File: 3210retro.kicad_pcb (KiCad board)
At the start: 2 copper layers, 44 x 115 mm, 404 parts, among them J901 MICRO_SD, P101 USB_OTG, P102 BAT, P103 DC, P105 EAR, P107 HEADPHONE, P109 RUMBLE, P301 SEPS525, P801 JTAG, Q201 BC817-40, Q801 BSS138, SW701 SW_PUSH, SW702 C, SW703 1, SW704 4ghi, SW705 7pqrs, SW706 -, SW707 2abc, SW708 5jkl, SW709 8tuv, SW710 UP, SW711 3def, SW712 6mno, SW713 9wxyz, SW714 *+, SW715 DOWN, SW716 0space, SW717 #up, U201 STM32F439NIH6, U202 TPS61046, U302 TPS61041DBV, U401 TPS62172, U402 MAX1555, U403 DRV8601, U404 LM4930, U405 TS5A22366, U406 MP34DT01TR, U407 MP34DT01TR, U801 A7, U802 SIM_SLOT, U901 ESP-12E, X101 ANT_GPS, X102 ANT_GSM, Y201 32kHz, Y202 24MHz, Y401 1M

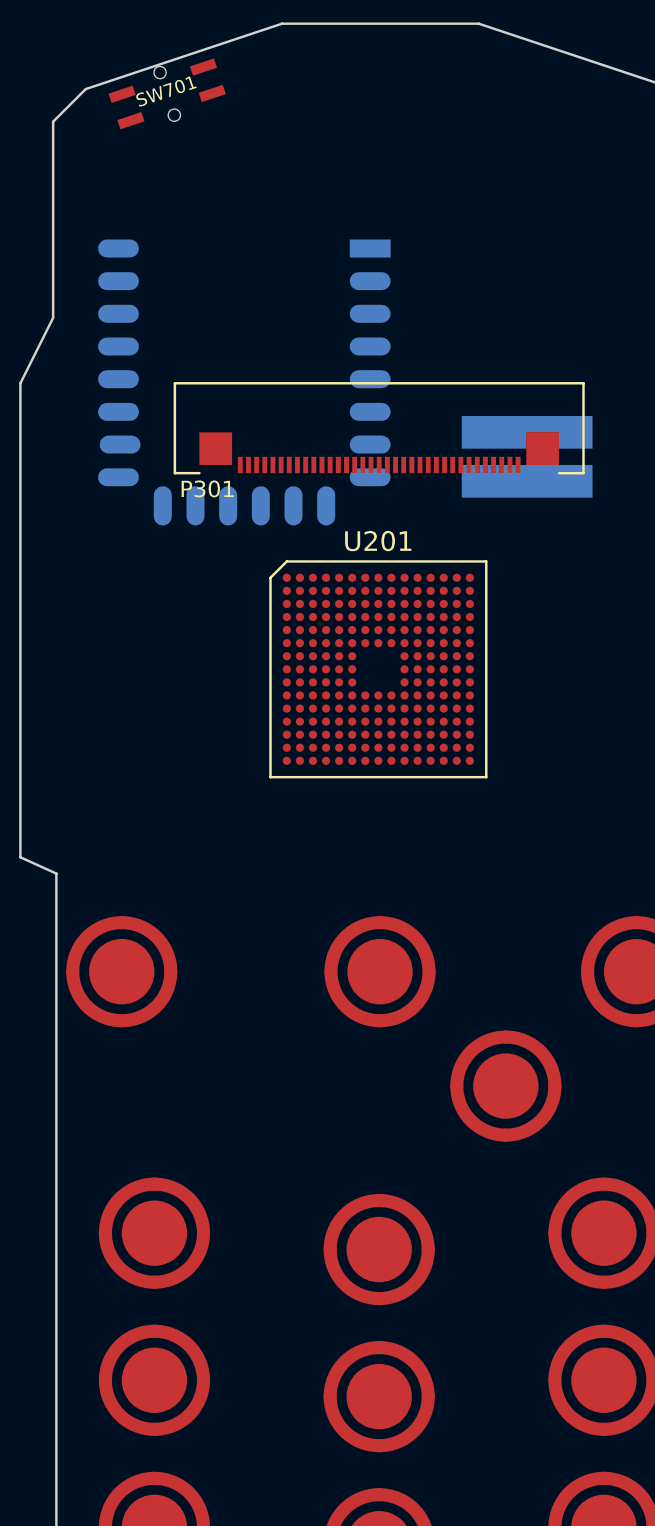
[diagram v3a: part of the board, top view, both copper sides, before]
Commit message: Started STM32 Fanout
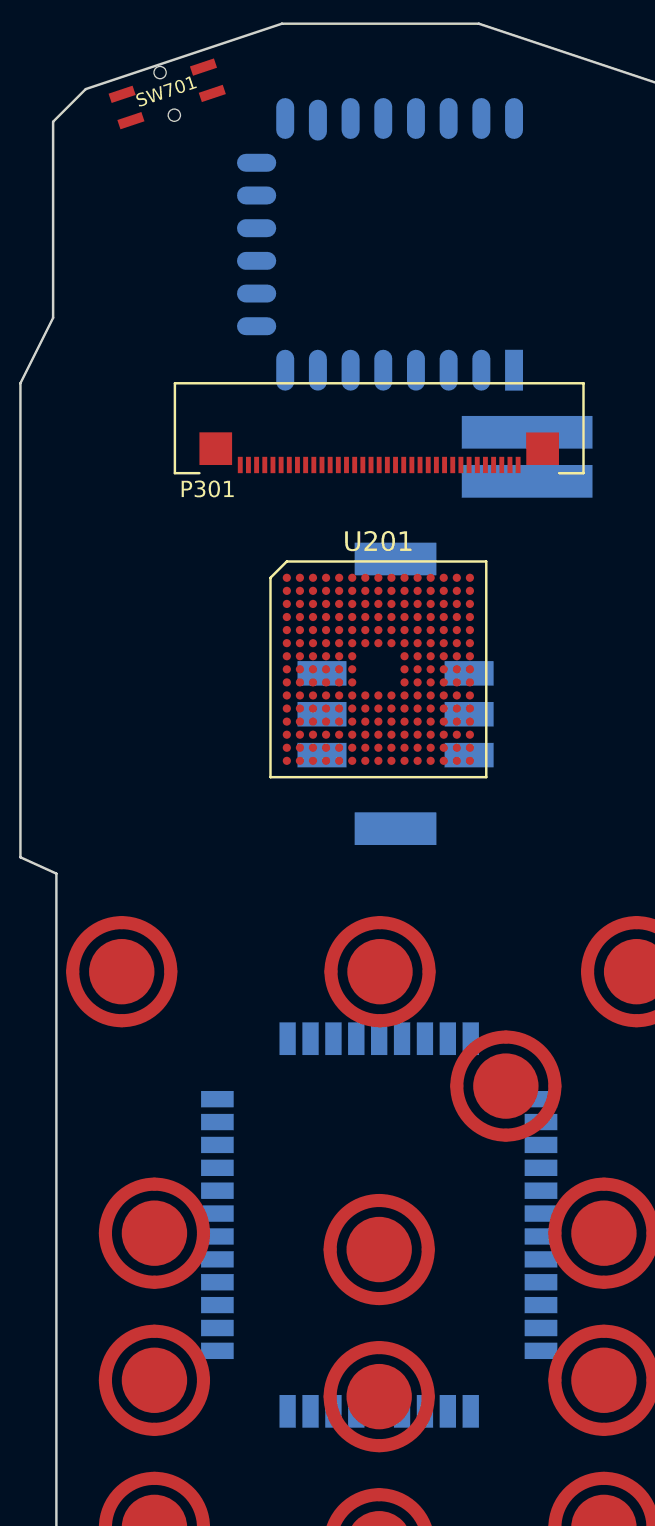
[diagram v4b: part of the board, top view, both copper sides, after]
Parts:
- moved U801 19.3 mm to (99.3, 117.6)
- moved U901 11.7 mm to (107.6, 64.6), turned to 90 degrees
- moved U802 5.76 mm to (100.3, 85.1), turned to 180 degrees
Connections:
- R803 pad 1: (no net) -> Net-(R803-Pad1)
- R804 pad 1: (no net) -> Net-(R804-Pad1)
- R805 pad 1: (no net) -> Net-(R805-Pad1)
- R806 pad 1: (no net) -> Net-(R806-Pad1)
- R807 pad 1: (no net) -> Net-(R807-Pad1)
- R808 pad 1: (no net) -> Net-(R808-Pad1)
- R809 pad 1: (no net) -> Net-(R809-Pad1)
- R810 pad 1: (no net) -> Net-(R810-Pad1)
- R813 pad 2: (no net) -> Net-(R813-Pad2)
- U404 pad 24: (no net) -> /Audio Amplifier/SPK_-
- U404 pad 25: (no net) -> /Audio Amplifier/SPK_+
- U405 pad D1: (no net) -> /Audio Amplifier/MIC_-
- U405 pad D3: (no net) -> /Audio Amplifier/MIC_+

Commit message: placed leds and corrected measurements
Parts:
- R234, R235: moved to B.Cu
- U201: footprint buttons:STM32F439NI -> buttons:STM32F439NI2
- moved C209 286.5 mm to (-100.7, 194.0)
- moved C218 285.6 mm to (-101.6, 180.4)
- moved C208 285.0 mm to (-106.6, 198.8)
- moved C207 283.3 mm to (-107.4, 190.7)
- moved C212 277.5 mm to (-94.0, 189.6)
- moved C220 274.0 mm to (-96.7, 179.1)
- moved C210 272.1 mm to (-98.9, 187.9)
- moved C225 271.7 mm to (-100.6, 174.2)
- moved C223 271.3 mm to (-95.9, 171.1)
- moved C221 269.5 mm to (-88.5, 176.4)
- moved C214 268.4 mm to (-90.0, 181.1)
- moved C222 265.4 mm to (-94.6, 176.0)
- moved C224 262.3 mm to (-91.0, 172.7)
- moved C216 262.2 mm to (-94.6, 194.3)
- moved C217 260.6 mm to (-89.4, 191.3)
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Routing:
- net (no net): track 0.00 -> 154.4 mm, vias 0 -> 37
- net GND: track 0.00 -> 45.7 mm, vias 0 -> 8
- net VCC: track 0.00 -> 41.9 mm, vias 0 -> 10
- net /Buttons and LEDs/KEY0: track 0.00 -> 34.8 mm, vias 0 -> 4
- net Net-(R234-Pad1): track 0.00 -> 11.5 mm
- net Net-(R237-Pad1): track 0.00 -> 5.67 mm, vias 0 -> 1
- net Net-(R247-Pad1): track 0.00 -> 5.13 mm, vias 0 -> 1
- net Net-(R236-Pad1): track 0.00 -> 5.03 mm, vias 0 -> 1
- net Net-(P801-Pad10): track 0.00 -> 4.95 mm, vias 0 -> 2
- net Net-(RP905-Pad2): track 0.00 -> 4.27 mm
- net Net-(RP905-Pad1): track 0.00 -> 4.07 mm, vias 0 -> 1
- net Net-(R248-Pad1): track 0.00 -> 3.77 mm, vias 0 -> 1
- net Net-(R246-Pad1): track 0.00 -> 3.57 mm, vias 0 -> 1
- net Net-(C206-Pad1): track 0.00 -> 3.49 mm, vias 0 -> 2
- net Net-(RP903-Pad5): track 0.00 -> 3.07 mm
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- added copper zone on F.Cu, net GND
- added copper zone on In1.Cu, net GND
- added copper zone on F.Cu, net VCC
- added copper zone on In2.Cu, net VCC
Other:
- board size 44 x 115 mm -> 44 x 118 mm
- copper layers 2 -> 4
- net class Default: clearance 0.2 -> 0.15; trace_width 0.25 -> 0.15; via_dia 0.6 -> 0.5; via_drill 0.4 -> 0.2
- net class SmallPower added: clearance 0.15, trace_width 0.2, via_dia 0.5, via_drill 0.2
- rule trace_clearance: 0.2 -> 0.15
- rule trace_min: 0.2 -> 0.15
- rule via_min_drill: 0.3 -> 0.2

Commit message: Created netlist with current components Foreward Annotation to Board
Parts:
- removed C221, C222, C223, C224, C225, C227, C306, C307, C308, C309, C423, C424, C425, C426: 100n, Capacitors_SMD:C_0603
- removed C226: 10u, Capacitors_SMD:C_0603
- removed C228: 1n, Capacitors_SMD:C_0603
- removed C229, C230, C231, C312: 1u, Capacitors_SMD:C_0603
- removed C310: 4u7C, Capacitors_SMD:C_0603
- removed C311: 10p, Capacitors_SMD:C_0603
- removed FI401: EMI_FILTER2, Choke_SMD:Choke_SMD_1206_Standard
- removed Q801: BSS138, TO_SOT_Packages_SMD:SOT-23
- removed R219, R220, R221, R222, R225, R226, R228, R229, R234, R235, R236, R237, R238, R239, R240, R241, R242, R243, R244, R245, R246, R247, R248, R816, R817, R818: 100, Resistors_SMD:R_0603
- removed R223, R224, R408, R409, R410, R412, R413, R414, R415: R, Resistors_SMD:R_0603
- removed R227: 10k, Resistors_SMD:R_0603
- removed R249, R416: 0, Resistors_SMD:R_0603
- removed R411, R417: 50k, Resistors_SMD:R_0603
- removed R418: 100k, Resistors_SMD:R_0603
- removed R419, R420: 1k, Resistors_SMD:R_0603
- removed R710, R712: 280, Resistors_SMD:R_0603
- removed R911, R912, R913, R915, R916: 10, Resistors_SMD:R_0603
- removed R914: 22, Resistors_SMD:R_0603
- removed RP901, RP902, RP903, RP904, RP905: 100, Resistors_SMD:R_Array_Convex_8x0602
- removed TP207, TP208, TP209, TP210, TP211, TP212, TP213, TP214, TP215, TP216, TP502, TP503, TP504, TP505, TP506, TP507, TP508, TP509, TP510, TP511, TP512, TP513, TP514, TP515, TP601, TP602, TP734, TP735, TP736, TP737, TP738, TP739, TP740, TP741, TP742, TP743, TP744, TP745, TP746, TP747, TP748, TP802, TP803, TP804, TP805, TP806, TP807, TP808, TP809, TP810, TP811, TP812, TP813, TP814, TP815, TP816, TP817, TP818, TP819, TP820, TP821, TP822, TP823, TP824, TP825, TP826, TP827, TP828, TP829, TP830, TP831, TP832, TP833, TP834, TP835, TP836, TP837, TP838, TP839, TP840, TP841, TP842, TP843, TP844, TP845, TP846, TP847, TP848, TP849, TP850, TP851, TP852, TP853, TP854, TP855, TP856, TP901, TP902, TP903, TP904, TP905, TP906, TP907, TP908, TP909, TP910, TP911, TP912: TP, buttons:TP
- removed U302: TPS61041DBV, TO_SOT_Packages_SMD:SOT-23
- removed U406, U407: MP34DT01TR, buttons:MP34DT01
- removed U802: SIM_SLOT, buttons:SIM
- removed Y201: 32kHz, Crystals:Crystal_SMD_SeikoEpson_MC146-4pin_6.7x1.5mm_HandSoldering
- removed Y202: 24MHz, Crystals:Crystal_SMD_SeikoEpson_MC146-4pin_6.7x1.5mm_HandSoldering
- removed Y401: 1M, Crystals:Crystal_SMD_SeikoEpson_MC146-4pin_6.7x1.5mm_HandSoldering
- added BT1001: LI_BAT, Pin_Headers:Pin_Header_Straight_1x02, F.Cu at (383.7, 45.1)
- added C1001: 1u, Capacitors_SMD:C_0603, F.Cu at (386.1, 76.7)
- added C1002: 1u, Capacitors_SMD:C_0603, F.Cu at (415.5, 47.7)
- added C1003: 2u2, Capacitors_SMD:C_0603, F.Cu at (378.8, 70.1)
- added C1004: 1u, Capacitors_SMD:C_0603, F.Cu at (420.6, 41.9)
- added C1005: 4u7, Capacitors_SMD:C_0603, F.Cu at (409.6, 53.4)
- added C1006: 2u2, Capacitors_SMD:C_0603, F.Cu at (399.6, 64.9)
- added C1007: 10uF, Capacitors_SMD:C_0603, F.Cu at (404.7, 59.2)
- added C1008: 4u7, Capacitors_SMD:C_0603, F.Cu at (391.2, 72.0)
- added C1009: 100nF, Capacitors_SMD:C_0402, F.Cu at (435.9, 47.1)
- added C1010: 1uF, Capacitors_SMD:C_0603, F.Cu at (396.3, 72.0)
- added C1011: 2u2, Capacitors_SMD:C_0603, F.Cu at (420.6, 47.7)
- added C1012: 1uF, Capacitors_SMD:C_0603, F.Cu at (425.7, 41.9)
- added C1013: 4u7, Capacitors_SMD:C_0603, F.Cu at (414.7, 53.4)
- added C1014: 220nF, Capacitors_SMD:C_0402, F.Cu at (420.0, 58.8)
- added C1015: 1uF, Capacitors_SMD:C_0603, F.Cu at (394.5, 66.2)
- added C1016: 100nF, Capacitors_SMD:C_0402, F.Cu at (424.9, 53.2)
- added C1017: 100n, Capacitors_SMD:C_0402, F.Cu at (430.0, 53.0)
- added C1018: 4u7, Capacitors_SMD:C_0603, F.Cu at (389.4, 66.2)
- added C1019: 100nF, Capacitors_SMD:C_0402, F.Cu at (420.0, 64.1)
- added C1020: 100n, Capacitors_SMD:C_0402, F.Cu at (414.9, 64.5)
- added C1021: 100n, Capacitors_SMD:C_0402, F.Cu at (409.8, 64.5)
- added C1022: 1u, Capacitors_SMD:C_0603, F.Cu at (415.5, 41.9)
- added C1023: 100n, Capacitors_SMD:C_0402, F.Cu at (430.8, 47.3)
- added C1024: 100n, Capacitors_SMD:C_0402, F.Cu at (435.9, 41.7)
- added C1025: 100n, Capacitors_SMD:C_0402, F.Cu at (401.4, 76.0)
- added C1026: 100n, Capacitors_SMD:C_0402, F.Cu at (406.5, 70.3)
- added C1027: 4u7, Capacitors_SMD:C_0603, F.Cu at (410.4, 47.7)
- added C1028: 4u7, Capacitors_SMD:C_0603, F.Cu at (381.0, 76.7)
- added C1029: 4u7, Capacitors_SMD:C_0603, F.Cu at (399.6, 59.2)
- added C1030: 4u7, Capacitors_SMD:C_0603, F.Cu at (384.3, 65.2)
- added C1031: 22uF, Capacitors_SMD:C_0603, F.Cu at (384.3, 59.5)
- added C1032: 22u, Capacitors_SMD:C_0603, F.Cu at (394.3, 54.7)
- added C1033: 22u, Capacitors_SMD:C_0603, F.Cu at (394.3, 49.0)
- added C1034: 22uF, Capacitors_SMD:C_0603, F.Cu at (400.2, 47.7)
- added C1035: 22u, Capacitors_SMD:C_0603, F.Cu at (400.2, 41.9)
- added C1036: 22u, Capacitors_SMD:C_0603, F.Cu at (405.3, 47.7)
- added C1037: 22u, Capacitors_SMD:C_0603, F.Cu at (405.3, 41.9)
- added C1038: 22u, Capacitors_SMD:C_0603, F.Cu at (410.4, 41.9)
- added C1039: 22u, Capacitors_SMD:C_0603, F.Cu at (399.4, 53.4)
- added C1040: 22u, Capacitors_SMD:C_0603, F.Cu at (389.4, 60.5)
- added C1041: 22u, Capacitors_SMD:C_0603, F.Cu at (375.9, 75.9)
- added C1042: 22u, Capacitors_SMD:C_0603, F.Cu at (383.9, 71.0)
- added C1043: 22u, Capacitors_SMD:C_0603, F.Cu at (394.5, 60.5)
- added C1044: 22u, Capacitors_SMD:C_0603, F.Cu at (404.5, 53.4)
- added C1101: 220n, Capacitors_SMD:C_0402, F.Cu at (502.1, 102.8)
- added C1102: 220n, Capacitors_SMD:C_0402, F.Cu at (497.0, 102.8)
- added C1103: 220n, Capacitors_SMD:C_0402, F.Cu at (502.1, 97.4)
- added C1104: 220n, Capacitors_SMD:C_0402, F.Cu at (497.0, 97.4)
- added C1105: 2u2, Capacitors_SMD:C_0603, F.Cu at (491.9, 97.6)
- added C1106: C, Capacitors_SMD:C_0402, F.Cu at (491.9, 103.2)
- added C1201: 220n, Capacitors_SMD:C_0402, F.Cu at (561.9, 7.59)
- added C1202: 220n, Capacitors_SMD:C_0402, F.Cu at (556.4, 13.1)
- added C1203: 220n, Capacitors_SMD:C_0402, F.Cu at (567.0, 2.24)
- added C1204: 220n, Capacitors_SMD:C_0402, F.Cu at (572.1, -3.11)
- added C1205: 220n, Capacitors_SMD:C_0402, F.Cu at (577.2, -8.46)
- added C1206: 220n, Capacitors_SMD:C_0402, F.Cu at (567.0, -3.11)
- added C1207: 220n, Capacitors_SMD:C_0402, F.Cu at (561.9, 12.9)
- added C1208: 4u7, Capacitors_SMD:C_0603, F.Cu at (536.0, 8.99)
- added C1209: 220n, Capacitors_SMD:C_0402, F.Cu at (577.2, -3.11)
- added C1210: 220n, Capacitors_SMD:C_0402, F.Cu at (551.3, 13.5)
- added C1211: 220n, Capacitors_SMD:C_0402, F.Cu at (572.1, 2.24)
- added C1212: 220n, Capacitors_SMD:C_0402, F.Cu at (530.9, 15.8)
- added C1213: 220n, Capacitors_SMD:C_0402, F.Cu at (561.9, -8.46)
- added C1214: 220n, Capacitors_SMD:C_0402, F.Cu at (536.0, 14.5)
- added C1215: 2u2, Capacitors_SMD:C_0603, F.Cu at (530.9, -1.23)
- added C1216: 220n, Capacitors_SMD:C_0402, F.Cu at (551.7, 2.84)
- added C1217: 22u, Capacitors_SMD:C_0603, F.Cu at (536.4, -8.26)
- added C1218: 220n, Capacitors_SMD:C_0402, F.Cu at (546.2, 13.9)
- added C1219: 220n, Capacitors_SMD:C_0402, F.Cu at (556.8, 7.79)
- added C1220: 22u, Capacitors_SMD:C_0603, F.Cu at (541.5, -8.26)
- added C1221: 22u, Capacitors_SMD:C_0603, F.Cu at (536.4, -2.51)
- added C1222: 220n, Capacitors_SMD:C_0402, F.Cu at (561.9, 2.24)
- added C1223: 2u2, Capacitors_SMD:C_0603, F.Cu at (541.5, -2.51)
- added C1224: 2u2, Capacitors_SMD:C_0603, F.Cu at (536.0, 3.24)
- added C1225: 2u2, Capacitors_SMD:C_0603, F.Cu at (546.6, -2.51)
- added C1226: 220n, Capacitors_SMD:C_0402, F.Cu at (556.8, -2.91)
- added C1227: 220n, Capacitors_SMD:C_0402, F.Cu at (572.1, -8.46)
- added C1228: 220n, Capacitors_SMD:C_0402, F.Cu at (567.0, -8.46)
- added C1229: 220n, Capacitors_SMD:C_0402, F.Cu at (556.8, 2.44)
- added C1230: 2u2, Capacitors_SMD:C_0603, F.Cu at (541.1, 3.24)
- added C1231: 220n, Capacitors_SMD:C_0402, F.Cu at (561.9, -3.11)
- added C1232: 220n, Capacitors_SMD:C_0402, F.Cu at (551.3, 8.19)
- added C1233: 220n, Capacitors_SMD:C_0402, F.Cu at (541.1, 14.3)
- added C1234: 2u2, Capacitors_SMD:C_0603, F.Cu at (551.7, -8.26)
- added C1235: 220n, Capacitors_SMD:C_0402, F.Cu at (546.2, 8.59)
- added C1236: 2u2, Capacitors_SMD:C_0603, F.Cu at (530.9, 4.52)
- added C1237: 2u2, Capacitors_SMD:C_0603, F.Cu at (530.9, 10.3)
- added C1238: 2u2, Capacitors_SMD:C_0603, F.Cu at (546.6, -8.26)
- added C1301: 220n, Capacitors_SMD:C_0402, F.Cu at (603.7, -8.46)
- added C1302: 220n, Capacitors_SMD:C_0402, F.Cu at (596.7, -2.71)
- added C1303: 2u2, Capacitors_SMD:C_0603, F.Cu at (586.5, -4.31)
- added C1304: 2u2, Capacitors_SMD:C_0603, F.Cu at (593.5, -8.26)
- added C1305: 220n, Capacitors_SMD:C_0402, F.Cu at (601.8, -2.91)
- added C1306: 220n, Capacitors_SMD:C_0402, F.Cu at (608.8, -8.46)
- added C1307: 10u, Capacitors_SMD:C_0603, F.Cu at (586.5, 1.44)
- added C1308: 10n, Capacitors_SMD:C_0603, F.Cu at (591.6, -2.51)
- added C1309: 100n, Capacitors_SMD:C_0402, F.Cu at (606.9, -3.11)
- added C501: 100n, Capacitors_SMD:C_0402, F.Cu at (552.5, 71.5)
- added C502: 470u, Capacitors_SMD:C_0603, F.Cu at (544.2, 66.2)
- added C503: 100n, Capacitors_SMD:C_0402, F.Cu at (539.2, 84.8)
- added C504: C, Capacitors_SMD:C_0402, F.Cu at (548.3, 82.4)
- added C505: C, Capacitors_SMD:C_0402, F.Cu at (548.3, 77.1)
- added C506: C, Capacitors_SMD:C_0402, F.Cu at (552.5, 76.9)
- added C507: C, Capacitors_SMD:C_0402, F.Cu at (544.2, 82.8)
- added C601: 100n, Capacitors_SMD:C_0402, F.Cu at (413.4, 103.3)
- added C602: 1p, Capacitors_SMD:C_0402, F.Cu at (401.5, 115.1)
- added C603: 2p4, Capacitors_SMD:C_0402, F.Cu at (417.6, 103.1)
- added C604: 1u, Capacitors_SMD:C_0603, F.Cu at (409.3, 95.8)
- added C605: 10u, Capacitors_SMD:C_0603, F.Cu at (413.4, 86.7)
- added C606: 100n, Capacitors_SMD:C_0402, F.Cu at (405.7, 112.5)
- added C808: 2u2, Capacitors_SMD:C_0603, F.Cu at (535.3, 34.4)
- added C809: 100n, Capacitors_SMD:C_0402, F.Cu at (547.8, 39.8)
- added C810: 220n, Capacitors_SMD:C_0402, F.Cu at (535.0, 56.8)
- added C811: 470n, Capacitors_SMD:C_0402, F.Cu at (556.1, 34.2)
- added C812: 470n, Capacitors_SMD:C_0402, F.Cu at (543.6, 45.3)
- added C813: 470n, Capacitors_SMD:C_0402, F.Cu at (539.2, 56.2)
- added C814: 2u2, Capacitors_SMD:C_0603, F.Cu at (531.2, 34.4)
- added C815: 2u2, Capacitors_SMD:C_0603, F.Cu at (515.2, 55.6)
- added C816: 470n, Capacitors_SMD:C_0402, F.Cu at (556.1, 39.6)
- added C817: 470n, Capacitors_SMD:C_0402, F.Cu at (547.8, 50.5)
- added C818: 2u2, Capacitors_SMD:C_0603, F.Cu at (531.2, 40.2)
- added C905: 220n, Capacitors_SMD:C_0402, F.Cu at (476.6, 41.7)
- added C906: 22u, Capacitors_SMD:C_0603, F.Cu at (464.2, 47.7)
- added C907: 100n, Capacitors_SMD:C_0402, F.Cu at (463.7, 58.8)
- added C908: 220n, Capacitors_SMD:C_0402, F.Cu at (480.8, 41.7)
- added C909: 220n, Capacitors_SMD:C_0402, F.Cu at (459.6, 61.7)
- added C910: 220n, Capacitors_SMD:C_0402, F.Cu at (451.3, 67.5)
- added C911: 220n, Capacitors_SMD:C_0402, F.Cu at (472.5, 52.8)
- added C912: 220n, Capacitors_SMD:C_0402, F.Cu at (480.8, 63.1)
- added C913: 220n, Capacitors_SMD:C_0402, F.Cu at (476.6, 47.1)
- added C914: 220n, Capacitors_SMD:C_0402, F.Cu at (463.7, 64.1)
- added C915: 220n, Capacitors_SMD:C_0402, F.Cu at (480.8, 47.1)
- added C916: 220n, Capacitors_SMD:C_0402, F.Cu at (468.3, 58.2)
- added C917: 220n, Capacitors_SMD:C_0402, F.Cu at (459.6, 67.1)
- added C918: 220n, Capacitors_SMD:C_0402, F.Cu at (484.9, 41.7)
- added C919: 220n, Capacitors_SMD:C_0402, F.Cu at (472.5, 58.2)
- added C920: 220n, Capacitors_SMD:C_0402, F.Cu at (467.9, 63.5)
- added C921: 220n, Capacitors_SMD:C_0402, F.Cu at (484.9, 47.1)
- added C922: 220n, Capacitors_SMD:C_0402, F.Cu at (489.1, 41.7)
- added C923: 22u, Capacitors_SMD:C_0603, F.Cu at (451.3, 56.4)
- added C924: 22u, Capacitors_SMD:C_0603, F.Cu at (447.1, 62.1)
- added C925: 220n, Capacitors_SMD:C_0402, F.Cu at (480.8, 52.4)
- added C926: 220n, Capacitors_SMD:C_0402, F.Cu at (463.7, 69.5)
- added C927: 220n, Capacitors_SMD:C_0402, F.Cu at (468.3, 52.8)
- added C928: 220n, Capacitors_SMD:C_0402, F.Cu at (493.2, 41.7)
- added C929: 220n, Capacitors_SMD:C_0402, F.Cu at (476.6, 57.8)
- added C930: 220n, Capacitors_SMD:C_0402, F.Cu at (480.8, 57.8)
- added C931: 220n, Capacitors_SMD:C_0402, F.Cu at (467.9, 68.9)
- added C932: 220n, Capacitors_SMD:C_0402, F.Cu at (489.1, 52.4)
- added C933: 220n, Capacitors_SMD:C_0402, F.Cu at (489.1, 47.1)
- added C934: 220n, Capacitors_SMD:C_0402, F.Cu at (484.9, 52.4)
- added C935: 220n, Capacitors_SMD:C_0402, F.Cu at (472.0, 68.9)
- added C936: 220n, Capacitors_SMD:C_0402, F.Cu at (493.2, 47.1)
- added C937: 220n, Capacitors_SMD:C_0402, F.Cu at (476.6, 63.1)
- added C938: 22u, Capacitors_SMD:C_0603, F.Cu at (447.1, 56.4)
- added C939: 22u, Capacitors_SMD:C_0603, F.Cu at (464.2, 41.9)
- added C940: 220n, Capacitors_SMD:C_0402, F.Cu at (472.0, 63.5)
- added D1001: D_Schottky, Diodes_SMD:DD-PAK_TO263_SingleDiode, F.Cu at (374.3, 49.5)
- added D201: BZT52-C5V1, Diodes_SMD:DD-PAK_TO263_SingleDiode, F.Cu at (374.3, -0.71)
- added D202: MMSD914LT, Diodes_SMD:DD-PAK_TO263_SingleDiode, F.Cu at (374.3, 20.4)
- added D203: S1A, Diodes_SMD:DD-PAK_TO263_SingleDiode, F.Cu at (400.0, -0.71)
- added D204: MMSD914LT, Diodes_SMD:DD-PAK_TO263_SingleDiode, F.Cu at (412.9, -0.71)
- added D205: ZHCS1000, Diodes_SMD:DD-PAK_TO263_SingleDiode, F.Cu at (387.2, 20.4)
- added D206: MMSD914LT, Diodes_SMD:DD-PAK_TO263_SingleDiode, F.Cu at (400.0, 20.4)
- added D207: MMSD914LT, Diodes_SMD:DD-PAK_TO263_SingleDiode, F.Cu at (387.2, -0.71)
- added D401: D_TVS_ALT, Diodes_SMD:DD-PAK_TO263_SingleDiode, F.Cu at (461.2, -0.71)
- added D402: D_TVS_ALT, Diodes_SMD:DD-PAK_TO263_SingleDiode, F.Cu at (474.1, -0.71)
- added D403: D_TVS_ALT, Diodes_SMD:DD-PAK_TO263_SingleDiode, F.Cu at (486.9, -0.71)
- added D801: D_Schottky, Diodes_SMD:DD-PAK_TO263_SingleDiode, F.Cu at (514.1, 42.0)
- added J1001: TEST_1P, NokiaRetroFit:TP, F.Cu at (387.1, 46.7)
- added J902: GND, NokiaRetroFit:TP, F.Cu at (446.7, 71.2)
- added J903: GND, NokiaRetroFit:TP, F.Cu at (445.6, 71.2)
- added J904: GND, NokiaRetroFit:TP, F.Cu at (484.5, 55.7)
- added J905: GND, NokiaRetroFit:TP, F.Cu at (485.6, 55.7)
- added J906: GND, NokiaRetroFit:TP, F.Cu at (447.8, 71.2)
- added J907: GND, NokiaRetroFit:TP, F.Cu at (449.8, 70.8)
- added J908: GND, NokiaRetroFit:TP, F.Cu at (450.9, 70.8)
- added J909: GND, NokiaRetroFit:TP, F.Cu at (452.0, 70.8)
- added J910: GND, NokiaRetroFit:TP, F.Cu at (453.1, 70.8)
- added J911: GND, NokiaRetroFit:TP, F.Cu at (454.2, 70.6)
- added J912: GND, NokiaRetroFit:TP, F.Cu at (455.3, 70.6)
- added J913: GND, NokiaRetroFit:TP, F.Cu at (456.4, 70.6)
- added J914: GND, NokiaRetroFit:TP, F.Cu at (454.2, 71.9)
- added J915: GND, NokiaRetroFit:TP, F.Cu at (483.4, 55.7)
- added J916: GND, NokiaRetroFit:TP, F.Cu at (460.8, 71.7)
- added J917: GND, NokiaRetroFit:TP, F.Cu at (459.7, 71.7)
- added J918: GND, NokiaRetroFit:TP, F.Cu at (458.6, 71.7)
- added J919: GND, NokiaRetroFit:TP, F.Cu at (460.3, 70.4)
- added J920: GND, NokiaRetroFit:TP, F.Cu at (459.2, 70.4)
- added J921: GND, NokiaRetroFit:TP, F.Cu at (457.5, 71.7)
- added J922: GND, NokiaRetroFit:TP, F.Cu at (456.4, 71.9)
- added J923: GND, NokiaRetroFit:TP, F.Cu at (458.1, 70.4)
- added J924: GND, NokiaRetroFit:TP, F.Cu at (455.3, 71.9)
- added L1001: 100R, Choke_SMD:Choke_SMD_1206_Standard, F.Cu at (379.0, 63.7)
- added L1002: 1u5H, Choke_SMD:Choke_SMD_1206_Standard, F.Cu at (389.0, 53.1)
- added L1003: 1u5H, Choke_SMD:Choke_SMD_1206_Standard, F.Cu at (394.9, 42.6)
- added L1004: 1u5H, Choke_SMD:Choke_SMD_1206_Standard, F.Cu at (383.5, 53.1)
- added L1005: 1u5H, Choke_SMD:Choke_SMD_1206_Standard, F.Cu at (389.4, 42.6)
- added L1006: 1u5H, Choke_SMD:Choke_SMD_1206_Standard, F.Cu at (370.6, 75.2)
- added L1201: 100R, Choke_SMD:Choke_SMD_1206_Standard, F.Cu at (531.1, -7.62)
- added L201: 4u7 / 3A, Choke_SMD:Choke_SMD_1206_Standard, F.Cu at (423.0, 1.97)
- added L202: 47u, Choke_SMD:Choke_SMD_1206_Standard, F.Cu at (409.2, 23.1)
- added L403: 120R@100MHz, Choke_SMD:Choke_SMD_1206_Standard, F.Cu at (473.3, 13.5)
- added L404: 120R@100MHz, Choke_SMD:Choke_SMD_1206_Standard, F.Cu at (499.0, -0.59)
- added L405: 120R@100MHz, Choke_SMD:Choke_SMD_1206_Standard, F.Cu at (484.6, 13.5)
- added L406: 120R@100MHz, Choke_SMD:Choke_SMD_1206_Standard, F.Cu at (499.0, -7.62)
- added L407: 120R@100MHz, Choke_SMD:Choke_SMD_1206_Standard, F.Cu at (471.7, 20.6)
- added L601: 1n3, Choke_SMD:Choke_SMD_1206_Standard, F.Cu at (399.0, 97.8)
- added L602: 2n2, Choke_SMD:Choke_SMD_1206_Standard, F.Cu at (404.5, 97.8)
- added L603: 0, Choke_SMD:Choke_SMD_1206_Standard, F.Cu at (377.5, 113.3)
- added L604: 1n8, Choke_SMD:Choke_SMD_1206_Standard, F.Cu at (383.0, 113.3)
- added L801: 100R, Choke_SMD:Choke_SMD_1206_Standard, F.Cu at (510.4, 56.2)
- added P104: DC, Pin_Headers:Pin_Header_Straight_2x01, F.Cu at (592.5, 27.6)
- added P106: SPEAKER, Pin_Headers:Pin_Header_Straight_2x01, F.Cu at (581.0, 36.8)
- added P108: RUMBLE, Pin_Headers:Pin_Header_Straight_1x02, F.Cu at (574.0, 27.6)
- added P601: ESP_DBG, Pin_Headers:Pin_Header_Straight_1x02, F.Cu at (391.9, 113.4)
- added P602: BT_DBG, Pin_Headers:Pin_Header_Straight_1x02, F.Cu at (399.1, 89.9)
- added P603: WL_DBG, Pin_Headers:Pin_Header_Straight_1x02, F.Cu at (391.4, 102.9)
- added P604: WL_RS232, Pin_Headers:Pin_Header_Straight_1x03, F.Cu at (392.3, 89.9)
- added P802: A7, Pin_Headers:Pin_Header_Straight_1x02, F.Cu at (527.0, 37.6)
- added P803: M4, Pin_Headers:Pin_Header_Straight_1x02, F.Cu at (522.6, 48.2)
- added Q202: PZTA42, TO_SOT_Packages_SMD:SOT-223, F.Cu at (430.6, -6.29)
- added Q203: BCP51, TO_SOT_Packages_SMD:SOT-223, F.Cu at (423.1, -6.29)
- added Q501: MMBF170, TO_SOT_Packages_SMD:SOT-23, F.Cu at (533.5, 85.3)
- added Q701: MMBF170, TO_SOT_Packages_SMD:SOT-23, F.Cu at (438.4, 119.1)
- added R1001: R, Resistors_SMD:R_0402, F.Cu at (409.8, 59.1)
- added R1002: R, Resistors_SMD:R_0402, F.Cu at (396.3, 77.6)
- added R1003: 470R, Resistors_SMD:R_0402, F.Cu at (419.8, 53.3)
- added R1004: 100K, Resistors_SMD:R_0402, F.Cu at (425.7, 47.6)
- added R1005: 0R, Resistors_SMD:R_0402, F.Cu at (391.2, 77.6)
- added R1006: 0R, Resistors_SMD:R_0402, F.Cu at (404.7, 64.8)
- added R1007: 0R, Resistors_SMD:R_0402, F.Cu at (430.8, 41.8)
- added R1008: 0R, Resistors_SMD:R_0402, F.Cu at (401.4, 70.6)
- added R1009: 0R, Resistors_SMD:R_0402, F.Cu at (414.9, 59.1)
- added R101: 0, Resistors_SMD:R_0402, F.Cu at (599.1, 24.3)
- added R1201: 0R, Resistors_SMD:R_0402, F.Cu at (541.1, 8.89)
- added R1202: 0R, Resistors_SMD:R_0402, F.Cu at (546.2, 3.14)
- added R1203: 0R, Resistors_SMD:R_0402, F.Cu at (556.8, -8.36)
- added R1204: 0R, Resistors_SMD:R_0402, F.Cu at (551.7, -2.61)
- added R1301: 200R, Resistors_SMD:R_0402, F.Cu at (598.6, -8.36)
- added R501: 22, Resistors_SMD:R_0402, F.Cu at (544.2, 77.4)
- added R502: 100, Resistors_SMD:R_0402, F.Cu at (548.3, 66.1)
- added R503: 0, Resistors_SMD:R_0402, F.Cu at (552.5, 66.1)
- added R504: 0, Resistors_SMD:R_0402, F.Cu at (548.3, 71.6)
- added R505: 100, Resistors_SMD:R_0402, F.Cu at (544.2, 71.8)
- added R603: 100k, Resistors_SMD:R_0402, F.Cu at (413.4, 92.3)
- added R604: 0, Resistors_SMD:R_0402, F.Cu at (425.9, 92.1)
- added R605: 0, Resistors_SMD:R_0402, F.Cu at (409.3, 101.5)
- added R606: 0, Resistors_SMD:R_0402, F.Cu at (417.6, 86.6)
- added R607: 0, Resistors_SMD:R_0402, F.Cu at (421.7, 97.7)
- added R608: 0, Resistors_SMD:R_0402, F.Cu at (408.9, 107.0)
- added R609: 0, Resistors_SMD:R_0402, F.Cu at (417.6, 97.7)
- added R610: 0, Resistors_SMD:R_0402, F.Cu at (425.9, 86.6)
- added R611: 0, Resistors_SMD:R_0402, F.Cu at (413.4, 97.9)
- added R612: 0, Resistors_SMD:R_0402, F.Cu at (397.4, 115.2)
- added R613: 0, Resistors_SMD:R_0402, F.Cu at (401.5, 109.6)
- added R614: 0, Resistors_SMD:R_0402, F.Cu at (421.7, 92.1)
- added R615: 0, Resistors_SMD:R_0402, F.Cu at (397.4, 109.6)
- added R616: 0, Resistors_SMD:R_0402, F.Cu at (404.8, 104.1)
- added R617: 0, Resistors_SMD:R_0402, F.Cu at (400.6, 104.1)
- added R618: 100k, Resistors_SMD:R_0402, F.Cu at (396.5, 104.1)
- added R703: 280, Resistors_SMD:R_0402, F.Cu at (448.3, 118.6)
- added R705: 280, Resistors_SMD:R_0402, F.Cu at (445.1, 124.2)
- added R707: 280, Resistors_SMD:R_0402, F.Cu at (449.3, 124.2)
- added TP1201: TP, NokiaRetroFit:TP, F.Cu at (542.3, 17.6)
- added TP1202: TP, NokiaRetroFit:TP, F.Cu at (539.0, 17.6)
- added TP1203: TP, NokiaRetroFit:TP, F.Cu at (540.1, 17.6)
- added TP1204: TP, NokiaRetroFit:TP, F.Cu at (541.2, 17.6)
- added TP1205: TP, NokiaRetroFit:TP, F.Cu at (546.3, 17.2)
- added TP1206: TP, NokiaRetroFit:TP, F.Cu at (545.2, 17.2)
- added TP1207: TP, NokiaRetroFit:TP, F.Cu at (549.2, 16.8)
- added TP1208: TP, NokiaRetroFit:TP, F.Cu at (544.1, 17.2)
- added U1001: PF3000, Housings_DFN_QFN:QFN-48-1EP_7x7mm_Pitch0.5mm, F.Cu at (372.1, 65.9)
- added U1301: LSM9DS1, NokiaRetroFit:LSM9DS1, F.Cu at (587.5, -9.11)
- added U301: TPS61041DBV, TO_SOT_Packages_SMD:SOT-23, F.Cu at (440.1, 108.1)
- added U504: A7, NokiaRetroFit:A7, F.Cu at (518.7, 75.9)
- added U505: SIM_SLOT, NokiaRetroFit:SIM, F.Cu at (536.0, 72.8)
- added U601: ESP-12E, NokiaRetroFit:ESP-12E, F.Cu at (372.0, 92.8)
- added U602: U.FL, NokiaRetroFit:Foil_Button, F.Cu at (140.5, 169.3)
- added U603: U.FL, NokiaRetroFit:Foil_Button, F.Cu at (141.8, 162.9)
- added U902: MT41K256M16HA-125, NokiaRetroFit:MT41K256M16HA-125, F.Cu at (453.6, 46.3)
- added Y601: ANT1/BT, SMD_Packages:1Pin, F.Cu at (405.2, 88.3)
- added Y602: ANT2/WL, SMD_Packages:1Pin, F.Cu at (371.1, 114.3)
- C201, C202, C203: value 22p -> 10u
- C204: value 22p -> C; footprint Capacitors_SMD:C_0603 -> Capacitors_SMD:C_0402
- C205, C206, C403: value C -> 100n; footprint Capacitors_SMD:C_0603 -> Capacitors_SMD:C_0402
- C207, C215, C217, C301, C302: footprint Capacitors_SMD:C_0603 -> Capacitors_SMD:C_0402
- C208, C209, C210, C216: value 100n -> 1n; footprint Capacitors_SMD:C_0603 -> Capacitors_SMD:C_0402
- C211: value 100n -> 330n
- C212: value 100n -> 2n2; footprint Capacitors_SMD:C_0603 -> Capacitors_SMD:C_0402
- C213: value 100n -> 47u; footprint Capacitors_SMD:C_0603 -> Capacitors_SMD:C_0805
- C214: value 100n -> 4p7; footprint Capacitors_SMD:C_0603 -> Capacitors_SMD:C_0402
- C218: value 100n -> 10u
- C219, C801, C803: value 100n -> 22p; footprint Capacitors_SMD:C_0603 -> Capacitors_SMD:C_0402
- C220, C305, C409: value 100n -> 1u
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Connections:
- C201 pad 1: Net-(C201-Pad1) -> +BATT_LIPO
- C202 pad 1: Net-(C202-Pad1) -> +BATT_LIPO
- C203 pad 1: Net-(C203-Pad1) -> +5V
- C204 pad 1: Net-(C204-Pad1) -> /Power and Battery/VDC+
- C204 pad 2: GND -> GNDREF
- C205 pad 1: /Controller/UART0 -> +BATT_LIPO
- C206 pad 1: Net-(C206-Pad1) -> +BATT_LIPO
- C207 pad 1: VCC -> +5V
- C208 pad 1: VCC -> +BATT_LIPO
- C209 pad 1: VCC -> +BATT_LIPO
- C210 pad 1: VCC -> +5V
- C211 pad 1: VCC -> Net-(C211-Pad1)
- C211 pad 2: GND -> Net-(C211-Pad2)
- C212 pad 1: VCC -> Net-(C212-Pad1)
- C213 pad 1: VCC -> Net-(C213-Pad1)
- C213 pad 2: GND -> GNDREF
- C214 pad 1: VCC -> Net-(C214-Pad1)
- C214 pad 2: GND -> Net-(C212-Pad1)
- C215 pad 1: VCC -> +BATT_LIPO
- C216 pad 1: VCC -> Net-(C216-Pad1)
- C216 pad 2: GND -> Net-(C216-Pad2)
- C217 pad 1: VCC -> Net-(C217-Pad1)
- C218 pad 1: VCC -> +BATT_LIPO
- C219 pad 1: VCC -> 4V_BST
- C220 pad 1: VCC -> 4V_BST
- C301 pad 1: VCC -> NVCC_1V8
- C302 pad 1: VCC -> NVCC_1V8
- C303 pad 1: VCC -> 4V_BST
- C304 pad 1: VCC -> 18V_BST
- C304 pad 2: GND -> Net-(C304-Pad2)
- C305 pad 1: VCC -> 18V_BST
- C401 pad 1: (no net) -> NVCC_3V3
- C401 pad 2: GND -> Net-(C401-Pad2)
- C402 pad 1: +BATT -> (no net)
- C403 pad 1: /Power and Battery/VDC+ -> NVCC_3V3
- C403 pad 2: GND -> Net-(C401-Pad2)
- C404 pad 1: Net-(C404-Pad1) -> VDD_SPK
- C405 pad 1: +5V -> VDD_SPK
- C405 pad 2: GND -> GNDA
- C406 pad 1: +5V -> +3.3VDAC
- C406 pad 2: GND -> GNDA
- C407 pad 1: Net-(C407-Pad1) -> /Audio Amplifier/RMBL+
- C407 pad 2: GNDA -> Net-(C407-Pad2)
- C408 pad 1: +3V3 -> /Audio Amplifier/MIC_BIAS
- C408 pad 2: GND -> GNDA
- C409 pad 1: +BATT -> +3.3VDAC
- C409 pad 2: GND -> GNDA
- C410 pad 1: /Audio Amplifier/RMBL+ -> (no net)
- C410 pad 2: Net-(C410-Pad2) -> GNDA
- C411 pad 1: Net-(C411-Pad1) -> +3.3VDAC
- C411 pad 2: GND -> GNDA
- C412 pad 1: Net-(C412-Pad1) -> +3.3VDAC
- C412 pad 2: GND -> GNDA
- C413 pad 1: +4V -> +3.3VDAC
- C413 pad 2: GND -> GNDA
- C414 pad 1: GND -> (no net)
- C415 pad 1: Net-(C415-Pad1) -> (no net)
- C415 pad 2: GND -> Net-(C415-Pad2)
- C416 pad 1: GND -> NVCC_3V3
- C416 pad 2: /Audio Amplifier/I2S_CCLK -> GND
- C417 pad 1: +3.3VDAC -> NVCC_3V3
- C417 pad 2: GNDA -> GND
- C418 pad 1: +3.3VDAC -> NVCC_3V3
- C418 pad 2: GNDA -> GND
- C419 pad 2: /Audio Amplifier/HPL -> (no net)
- C420 pad 1: +3.3VDAC -> NVCC_3V3
- C420 pad 2: GNDA -> GND
- C421 pad 1: +3.3VDAC -> /Audio Amplifier/HPR
- C422 pad 1: Net-(C422-Pad1) -> /Audio Amplifier/HPL
- C422 pad 2: /Audio Amplifier/HPR -> GNDA
- C801 pad 1: +4V -> (no net)
- C802 pad 1: +4V -> (no net)
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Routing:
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- removed copper zone on F.Cu, net GND
- removed copper zone on F.Cu, net VCC

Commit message: Startet routing DDR3. Some things need to be cleared before routign process an begin
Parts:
- U901: footprint NokiaRetroFit:MT41K256M16HA-125 -> NokiaRetroFit:FBGA_96_x16
- U902: footprint NokiaRetroFit:MT41K256M16HA-125 -> NokiaRetroFit:FBGA_96_x16; moved to B.Cu
- moved U902 349.4 mm to (107.1, 91.6)
- moved U602 226.0 mm to (360.7, 118.5)
- moved U603 216.4 mm to (353.6, 118.5)
- moved R1007 70.4 mm to (373.5, 82.7)
- moved U405 69.2 mm to (453.2, 31.4)
- moved C1004 65.7 mm to (368.4, 81.8)
- moved R301 61.2 mm to (427.4, 112.8)
- moved C903 61.0 mm to (446.0, 74.6)
- moved L404 60.7 mm to (442.6, 22.1)
- moved R1004 58.7 mm to (378.6, 82.7)
- moved C1036 57.7 mm to (358.2, 80.9)
- moved J915 57.2 mm to (430.0, 76.2)
- moved R211 57.0 mm to (399.0, 36.0)
- moved C408 56.2 mm to (471.9, 25.5)
- moved R610 54.1 mm to (383.8, 120.4)
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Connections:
- C1105 pad 1: (no net) -> Net-(C1105-Pad1)
- C801 pad 1: (no net) -> Net-(C801-Pad1)
- C802 pad 1: (no net) -> Net-(C802-Pad1)
- C803 pad 1: (no net) -> Net-(C803-Pad1)
- C804 pad 1: (no net) -> Net-(C804-Pad1)
- C807 pad 1: (no net) -> Net-(C807-Pad1)
- C814 pad 1: (no net) -> Net-(C814-Pad1)
- P101 pad 2: (no net) -> /Controller/D-
- P101 pad 3: (no net) -> /Controller/D+
- P101 pad 4: (no net) -> /Controller/USB_OTG_ID
- P801 pad 4: (no net) -> Net-(P801-Pad4)
- P801 pad 6: (no net) -> Net-(P801-Pad6)
- P802 pad 1: (no net) -> Net-(P802-Pad1)
- P802 pad 2: (no net) -> Net-(P802-Pad2)
- P803 pad 1: (no net) -> Net-(P803-Pad1)
- P803 pad 2: (no net) -> Net-(P803-Pad2)
- R1301 pad 2: (no net) -> Net-(R1301-Pad2)
- R401 pad 2: (no net) -> /Audio Amplifier/RMBL_PWM
- R505 pad 1: (no net) -> /Controller/GPS_TX
- R707 pad 2: (no net) -> /Buttons and LEDs/LEDPWM
- R802 pad 1: (no net) -> Net-(R802-Pad1)
- R803 pad 1: (no net) -> Net-(R803-Pad1)
- R806 pad 2: (no net) -> Net-(R806-Pad2)
- R810 pad 2: (no net) -> Net-(R810-Pad2)
- R811 pad 2: (no net) -> Net-(R811-Pad2)
- R812 pad 2: (no net) -> Net-(R812-Pad2)
- R814 pad 2: (no net) -> Net-(R814-Pad2)
- R908 pad 2: (no net) -> Net-(R908-Pad2)
- R910 pad 2: (no net) -> Net-(R910-Pad2)
- U1001 pad 1: (no net) -> /Controller/CPU Power Control/~PMIC_INT
- U1001 pad 2: (no net) -> /Controller/PMIC_SD_VSEL
- U1001 pad 4: (no net) -> /Controller/CPU Power Control/PMIC_STBY_REQ
- U1001 pad 45: (no net) -> I2C1_SDA
- U1001 pad 46: (no net) -> I2C1_SCL
- U801 pad AA24: (no net) -> /Controller/DDR3 RAM /DQM2
- U801 pad AB14: (no net) -> /Controller/DDR3 RAM /SDWE
- U801 pad AB15: (no net) -> /Controller/DDR3 RAM /RAS
- U801 pad AB16: (no net) -> /Controller/DDR3 RAM /DRAM_ADDR1
- U801 pad AB17: (no net) -> /Controller/DDR3 RAM /SDCKE0
- U801 pad AB18: (no net) -> /Controller/DDR3 RAM /DRAM_ADDR14
- U801 pad AB19: (no net) -> /Controller/DDR3 RAM /DRAM_ADDR0
- U801 pad AB21: (no net) -> /Controller/DDR3 RAM /DRAM_ADDR4
- U801 pad AB23: (no net) -> /Controller/DDR3 RAM /CS0
- U801 pad AB24: (no net) -> /Controller/DDR3 RAM /DRAM_DATA22
- U801 pad AB25: (no net) -> /Controller/DDR3 RAM /DRAM_DATA21
- U801 pad AC14: (no net) -> /Controller/DDR3 RAM /CAS
- U801 pad AC16: (no net) -> /Controller/DDR3 RAM /ODT0
- U801 pad AC18: (no net) -> /Controller/DDR3 RAM /DRAM_ADDR2
- U801 pad AC20: (no net) -> /Controller/DDR3 RAM /DRAM_ADDR3
- U801 pad AC24: (no net) -> /Controller/DDR3 RAM /DRAM_DATA23
- U801 pad AC25: (no net) -> /Controller/DDR3 RAM /DRAM_DATA20
- U801 pad AD13: (no net) -> /Controller/DDR3 RAM /DRAM_DATA14
- U801 pad AD14: (no net) -> /Controller/DDR3 RAM /DRAM_DATA13
- U801 pad AD15: (no net) -> /Controller/DDR3 RAM /SDQS1_P
- U801 pad AD16: (no net) -> /Controller/DDR3 RAM /DRAM_DATA11
- U801 pad AD17: (no net) -> /Controller/DDR3 RAM /DQM1
- U801 pad AD18: (no net) -> /Controller/DDR3 RAM /DRAM_DATA6
- U801 pad AD19: (no net) -> /Controller/DDR3 RAM /DRAM_DATA5
- U801 pad AD20: (no net) -> /Controller/DDR3 RAM /DQM0
- U801 pad AD23: (no net) -> /Controller/DDR3 RAM /DRAM_DATA1
- U801 pad AE13: (no net) -> /Controller/DDR3 RAM /DRAM_DATA15
- U801 pad AE14: (no net) -> /Controller/DDR3 RAM /DRAM_DATA8
- U801 pad AE15: (no net) -> /Controller/DDR3 RAM /SDQS1_N
- U801 pad AE16: (no net) -> /Controller/DDR3 RAM /DRAM_DATA12
- U801 pad AE17: (no net) -> /Controller/DDR3 RAM /DRAM_DATA10
- U801 pad AE18: (no net) -> /Controller/DDR3 RAM /DRAM_DATA9
- U801 pad AE19: (no net) -> /Controller/DDR3 RAM /DRAM_DATA7
- U801 pad AE20: (no net) -> /Controller/DDR3 RAM /DRAM_DATA2
- U801 pad AE22: (no net) -> /Controller/DDR3 RAM /DRAM_DATA4
- U801 pad AE23: (no net) -> /Controller/DDR3 RAM /DRAM_DATA3
- U801 pad N23: (no net) -> /Controller/DDR3 RAM /SDBA2
- U801 pad N24: (no net) -> /Controller/DDR3 RAM /DRAM_DATA25
- U801 pad N25: (no net) -> /Controller/DDR3 RAM /DRAM_DATA27
- U801 pad P22: (no net) -> /Controller/DDR3 RAM /SDBA1
- U801 pad P23: (no net) -> /Controller/DDR3 RAM /DRAM_ADDR13
- U801 pad P24: (no net) -> /Controller/DDR3 RAM /DQM3
- U801 pad P25: (no net) -> /Controller/DDR3 RAM /DRAM_DATA26
- U801 pad R22: (no net) -> /Controller/DDR3 RAM /SDBA0
- U801 pad R24: (no net) -> /Controller/DDR3 RAM /DRAM_DATA29
- U801 pad R25: (no net) -> /Controller/DDR3 RAM /DRAM_DATA24
- U801 pad T22: (no net) -> /Controller/DDR3 RAM /DRAM_ADDR12
- U801 pad T23: (no net) -> /Controller/DDR3 RAM /DRAM_ADDR10
- U801 pad T24: (no net) -> /Controller/DDR3 RAM /SDQS3_P
- U801 pad T25: (no net) -> /Controller/DDR3 RAM /SDQS3_N
- U801 pad U22: (no net) -> /Controller/DDR3 RAM /DRAM_ADDR11
- U801 pad U24: (no net) -> /Controller/DDR3 RAM /DRAM_DATA30
- U801 pad U25: (no net) -> /Controller/DDR3 RAM /DRAM_DATA28
- U801 pad V22: (no net) -> /Controller/DDR3 RAM /DRAM_ADDR6
- U801 pad V23: (no net) -> /Controller/DDR3 RAM /DRAM_ADDR9
- U801 pad V24: (no net) -> /Controller/DDR3 RAM /DRAM_DATA31
- U801 pad V25: (no net) -> /Controller/DDR3 RAM /DRAM_DATA18
- U801 pad W22: (no net) -> /Controller/DDR3 RAM /DRAM_ADDR8
- U801 pad W24: (no net) -> /Controller/DDR3 RAM /DRAM_DATA17
- U801 pad W25: (no net) -> /Controller/DDR3 RAM /DRAM_DATA19
- U801 pad Y22: (no net) -> /Controller/DDR3 RAM /DRAM_ADDR7
- U801 pad Y23: (no net) -> /Controller/DDR3 RAM /DRAM_ADDR5
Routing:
- net /Buttons and LEDs/KEYPAD_COL0: track 34.8 -> 0.00 mm, vias 4 -> 0
- net /Controller/DDR3 RAM /DRAM_ADDR7: track 0.00 -> 19.7 mm, vias 0 -> 1
- net /Controller/DDR3 RAM /DRAM_ADDR13: track 0.00 -> 15.4 mm, vias 0 -> 1
- net (no net): track 11.5 -> 0.00 mm
- net /Controller/DDR3 RAM /DRAM_DATA17: track 0.00 -> 3.09 mm
- net /Controller/DDR3 RAM /SDQS3_P: track 0.00 -> 3.05 mm
- net /Controller/DDR3 RAM /DRAM_DATA6: track 0.00 -> 3.00 mm
- net /Controller/DDR3 RAM /DRAM_DATA13: track 0.00 -> 3.00 mm
- net /Controller/DDR3 RAM /SDQS1_P: track 0.00 -> 2.98 mm
- net /Controller/DDR3 RAM /DQM3: track 0.00 -> 2.98 mm
- net /Controller/DDR3 RAM /DRAM_DATA31: track 0.00 -> 2.98 mm
- net /Controller/DDR3 RAM /DQM1: track 0.00 -> 2.94 mm
- net /Controller/DDR3 RAM /DRAM_DATA29: track 0.00 -> 2.92 mm
- net /Controller/DDR3 RAM /DRAM_DATA5: track 0.00 -> 2.86 mm
- net /Controller/DDR3 RAM /DRAM_DATA0: track 0.00 -> 2.78 mm
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- added copper zone on BOT_GND, net GND
- added copper zone on TOP_GND, net GND
- removed copper zone on In1.Cu, net GND
- removed copper zone on In2.Cu, net VCC
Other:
- copper layers 4 -> 8
- net class DDR_external added: clearance 0.1, trace_width 0.125, via_dia 0.5, via_drill 0.2
- rule pad_to_mask_clearance: 0.2 -> 0.1
- rule trace_min: 0.15 -> 0.075

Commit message: Routing DDR3: connecting all signals
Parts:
- moved C908 366.9 mm to (99.4, 96.1)
- moved R906 360.2 mm to (97.1, 96.0)
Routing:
- net NVCC_DRAM: track 0.00 -> 35.3 mm, vias 0 -> 11
- net /Controller/DDR3 RAM /DRAM_ADDR6: track 0.00 -> 22.3 mm, vias 1 -> 2
- net /Controller/DDR3 RAM /DRAM_ADDR11: track 0.00 -> 22.3 mm, vias 1 -> 2
- net /Controller/DDR3 RAM /DRAM_ADDR13: track 15.4 -> 37.5 mm, vias 1 -> 2
- net /Controller/DDR3 RAM /DRAM_ADDR8: track 0.00 -> 21.4 mm, vias 1 -> 2
- net /Controller/DDR3 RAM /DRAM_ADDR1: track 0.00 -> 21.2 mm, vias 1 -> 2
- net /Controller/DDR3 RAM /DRAM_ADDR14: track 0.00 -> 20.6 mm, vias 1 -> 2
- net /Controller/DDR3 RAM /DRAM_ADDR7: track 19.7 -> 40.0 mm, vias 1 -> 2
- net /Controller/DDR3 RAM /DRAM_ADDR12: track 0.00 -> 20.0 mm, vias 1 -> 2
- net /Controller/DDR3 RAM /SDWE: track 0.00 -> 19.7 mm, vias 1 -> 2
- net /Controller/DDR3 RAM /DRAM_ADDR2: track 0.00 -> 19.7 mm, vias 1 -> 2
- net /Controller/DDR3 RAM /DRAM_ADDR0: track 0.00 -> 18.9 mm, vias 1 -> 2
- net /Controller/DDR3 RAM /DRAM_ADDR9: track 0.00 -> 18.6 mm, vias 2 -> 4
- net /Controller/DDR3 RAM /CAS: track 0.00 -> 18.3 mm, vias 1 -> 2
- net /Controller/DDR3 RAM /DRAM_ADDR4: track 0.00 -> 18.2 mm, vias 1 -> 2
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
